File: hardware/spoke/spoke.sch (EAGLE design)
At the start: 22 parts, among them IC1 7805, J1 AVR_SPI_PRG_6PTH, J2 POWER_JACKPTH, U1 ATMEGA328P_PDIP, U2 AT25M01-SHM-B, U3 NRF24L01+

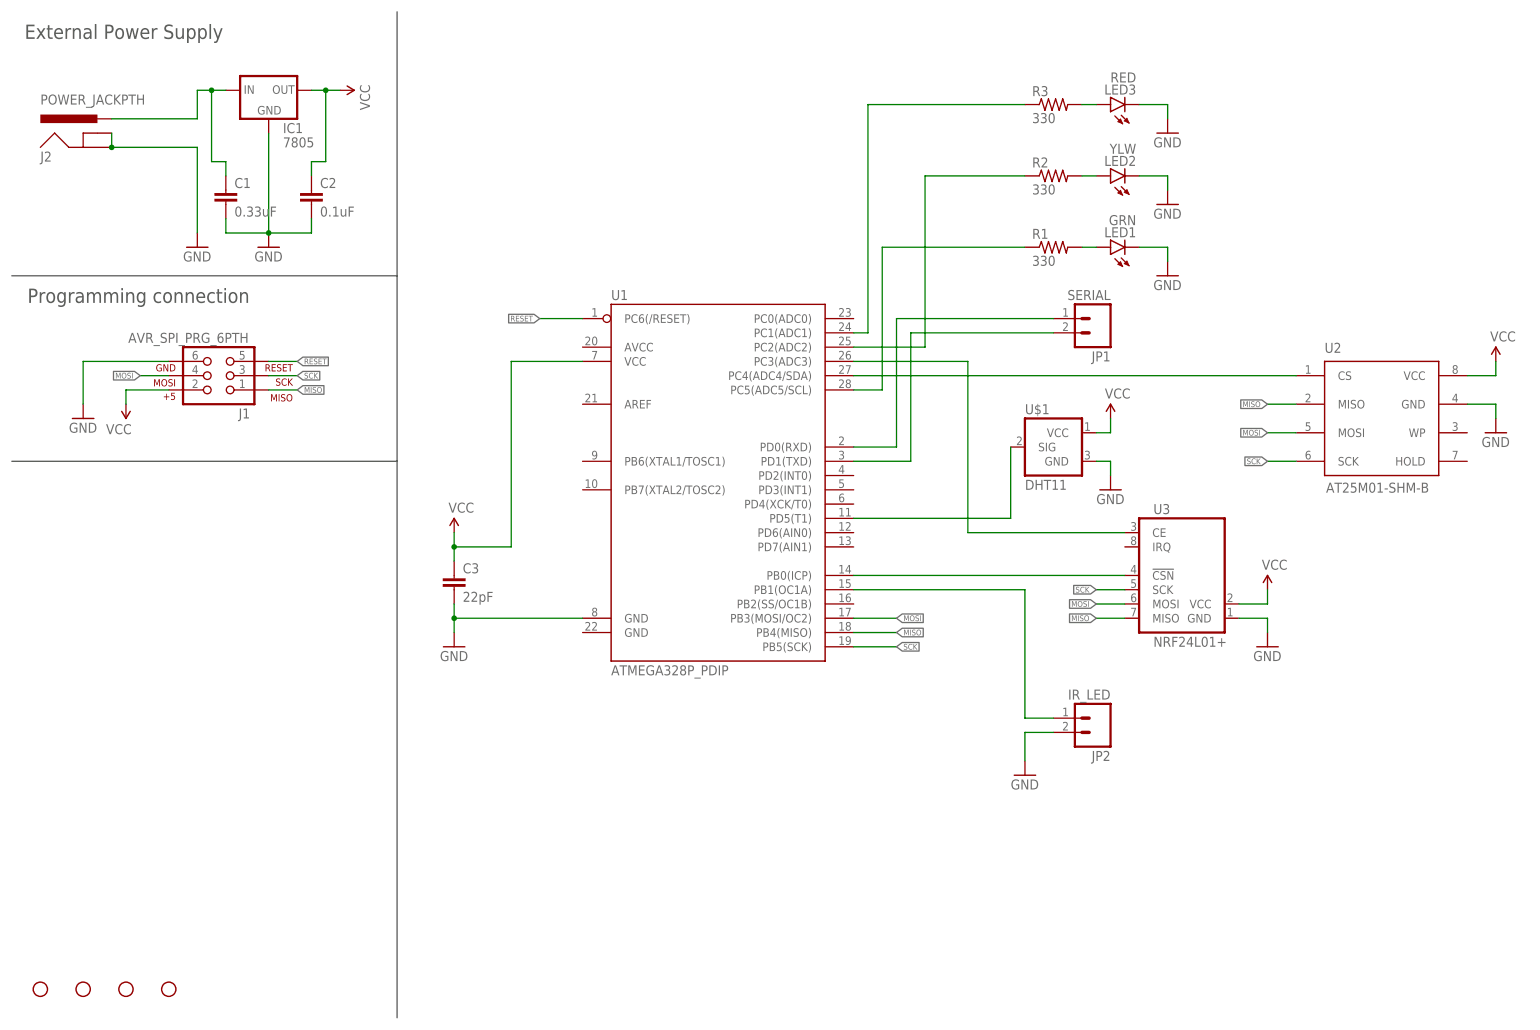
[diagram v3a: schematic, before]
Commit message: MOAR SMDs and 3.3v supply fixes
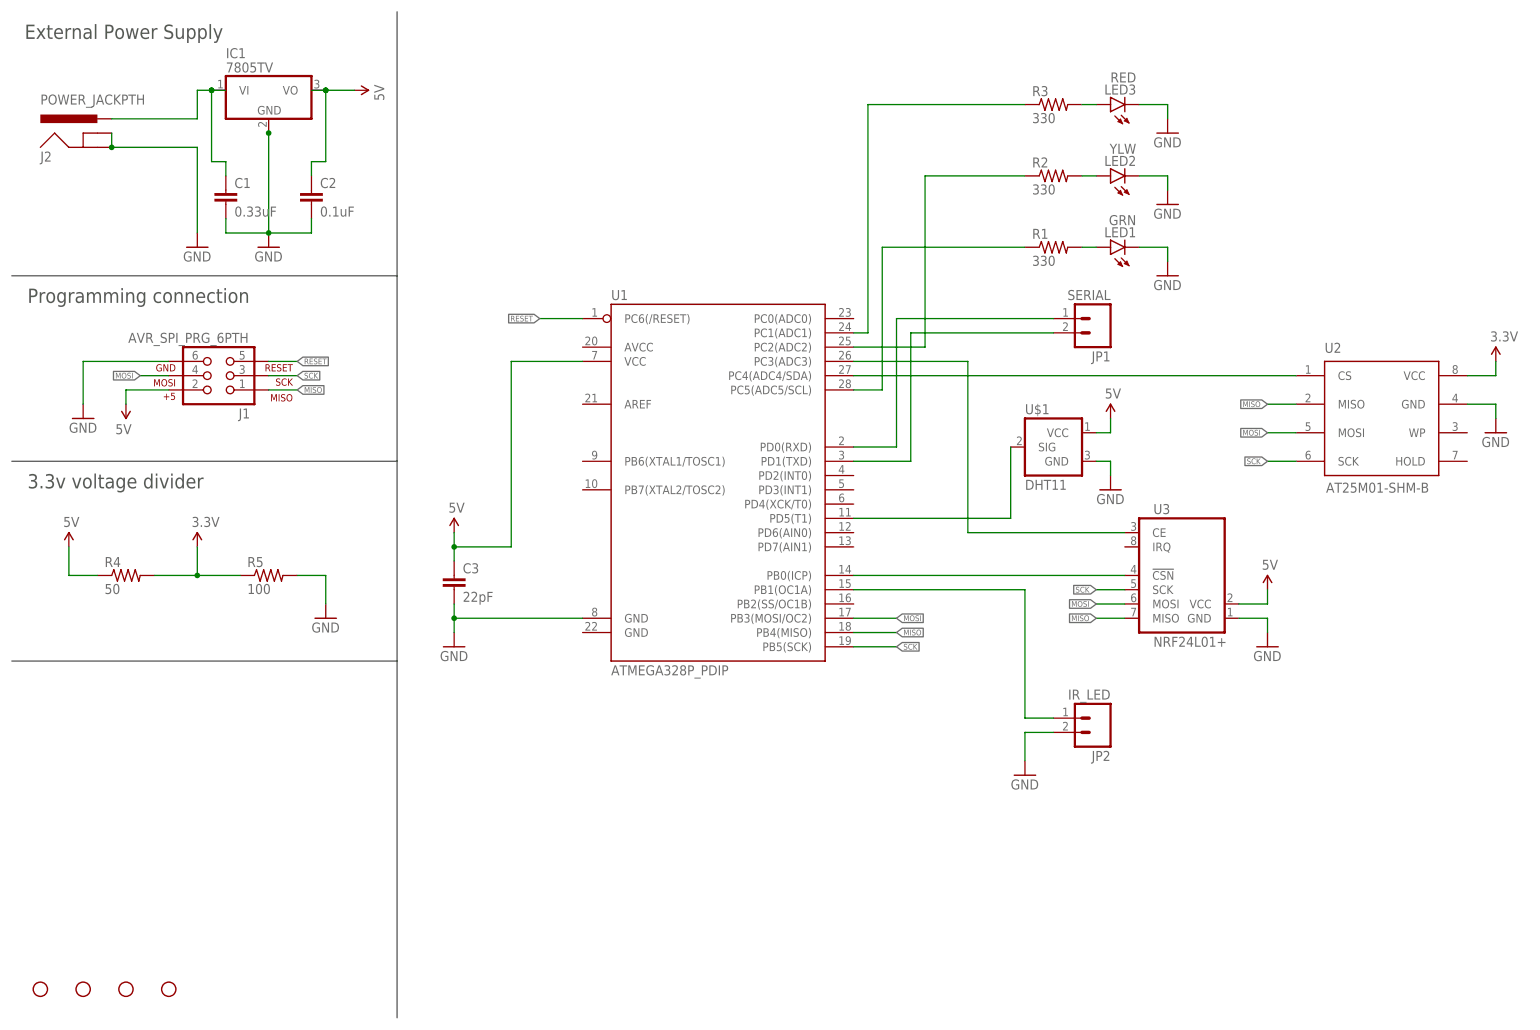
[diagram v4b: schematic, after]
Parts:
- added R4: 50, SparkFun-Passives:RESISTOR2010
- added R5: 100, SparkFun-Passives:RESISTOR2010
- C3: device SparkFun-Capacitors:CAPEZ -> SparkFun-Passives:CAP0805
- IC1: value 7805 -> 7805TV; device SparkFun-PowerIC:V_REG_78XXSINK -> linear:7805TV
- LED1, LED2, LED3: device SparkFun-LED:LED3MM -> SparkFun-LED:LED1206
- R1, R2, R3: device SparkFun-Passives:RESISTOREZ -> SparkFun-Passives:RESISTOR1206
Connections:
- removed net VCC: C2.1, C3.1, IC1.OUT, J1.2, U$1.VCC, U1.VCC, U2.VCC, U3.VCC
- new net 3.3V: R4.2, R5.1, U2.VCC
- new net 5V: C2.1, C3.1, IC1.VO, J1.2, R4.1, U$1.VCC, U1.VCC, U3.VCC
- net GND: now also R5.2
- net N$14: now also IC1.VI; no longer IC1.IN
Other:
- note added: "3.3v voltage divider"

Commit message: Update schematic from todos
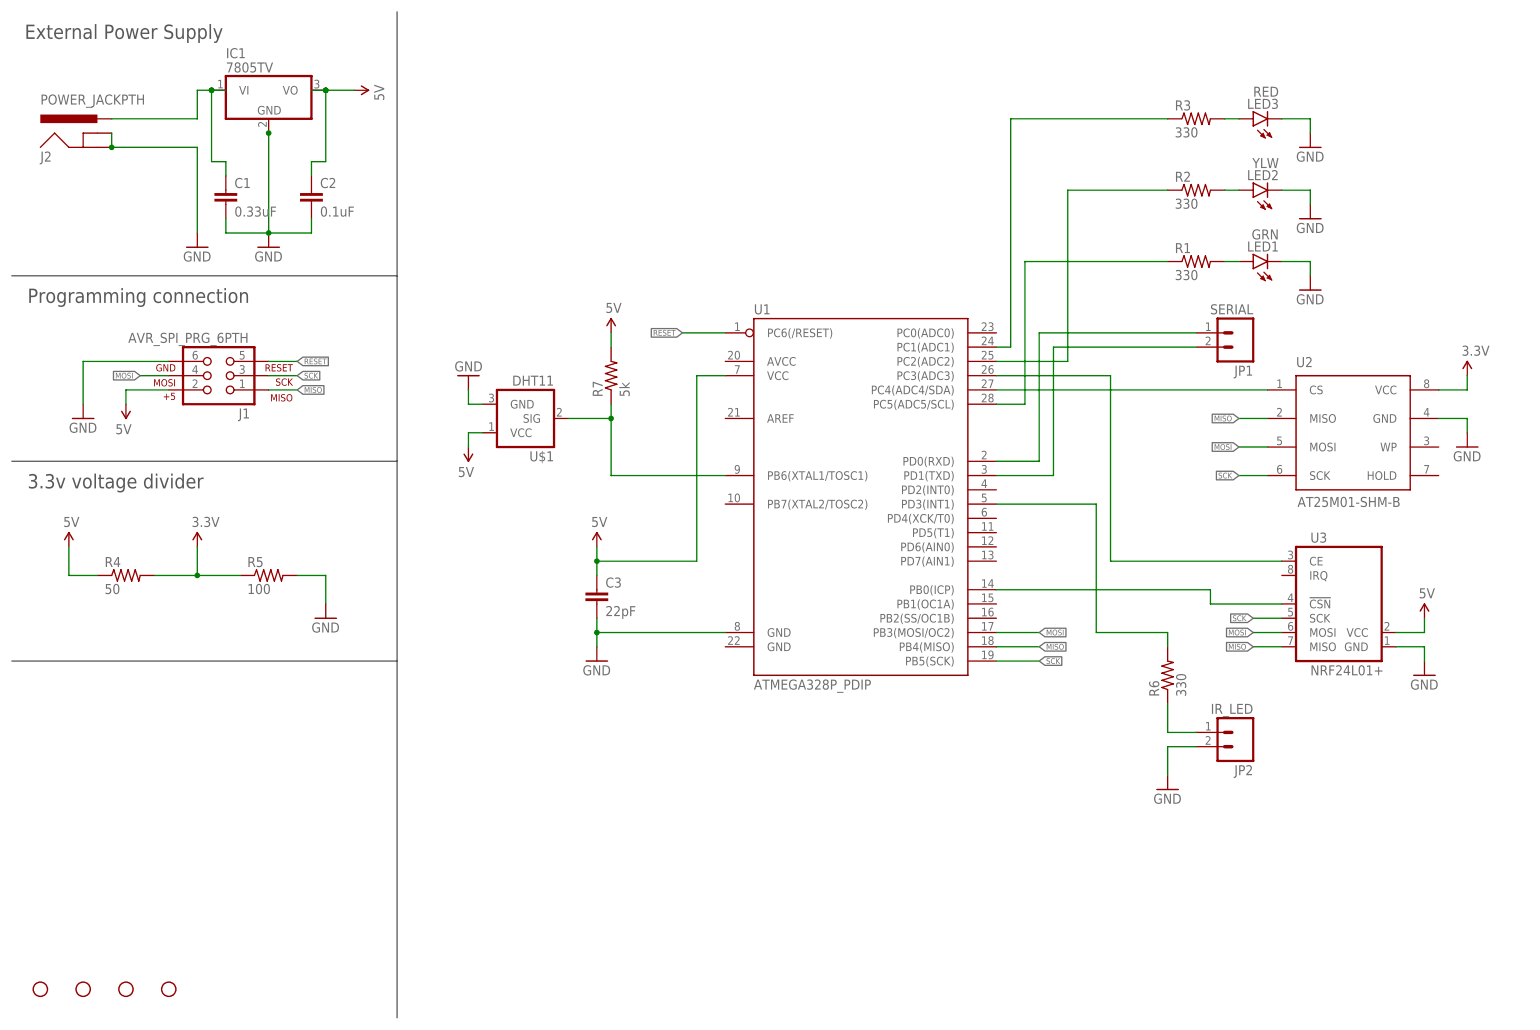
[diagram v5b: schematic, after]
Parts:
- added R6: 330, SparkFun-Passives:RESISTOR1206
- added R7: 5k, SparkFun-Passives:RESISTOR1206
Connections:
- removed net N$6: U$1.SIG, U1.PD5(T1)
- new net N$15: JP2.1, R6.1
- new net N$16: R6.2, U1.PD3(INT1)
- net 5V: now also R7.2
- net N$1: now also R7.1, U$1.SIG, U1.PB6(XTAL1/TOSC1); no longer JP2.1, U1.PB1(OC1A)
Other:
- moved on the sheet: C3, JP1, JP2, LED1, LED2, LED3, R1, R2, R3, U$1, U1, U2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

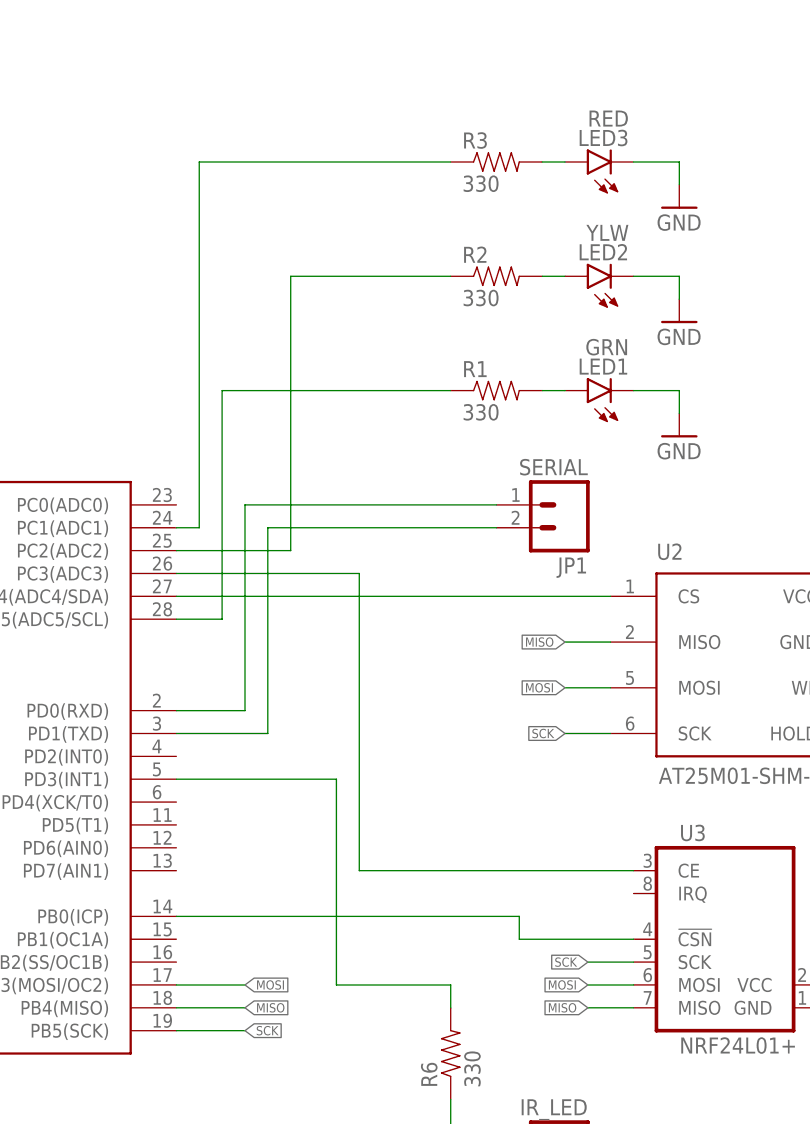
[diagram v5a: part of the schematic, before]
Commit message: Adjust schematic. Begin routing.
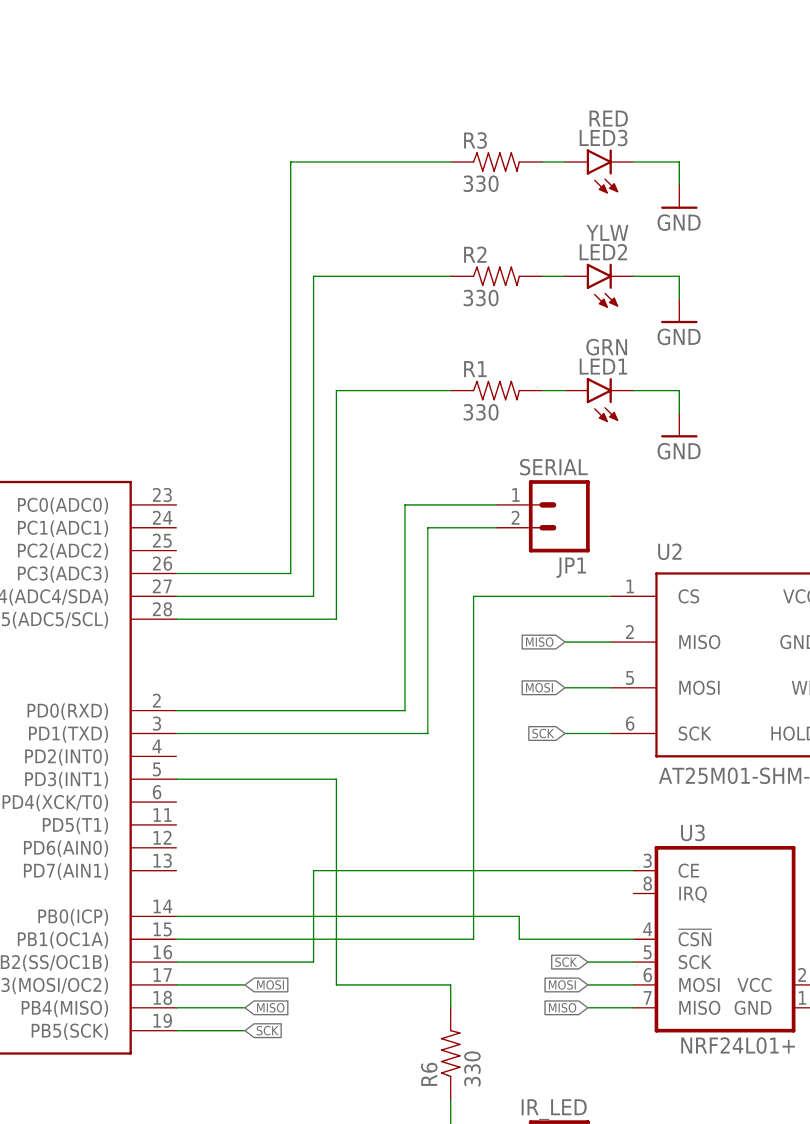
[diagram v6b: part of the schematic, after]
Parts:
- R1, R2, R3, R6, R7: device SparkFun-Passives:RESISTOR1206 -> SparkFun-Resistors:RESISTOR0805-RES
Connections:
- removed net N$13: R3.1, U1.PC1(ADC1)
- new net N$6: U1.PB1(OC1A), U2.CS
- net N$3: now also R2.1; no longer U2.CS
- net N$5: now also R3.1; no longer U3.CE
- net N$9: now also U1.PB2(SS/OC1B), U3.CE; no longer R2.1, U1.PC2(ADC2)
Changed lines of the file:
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@@
 <part name="GND8" library="SparkFun-Aesthetics" deviceset="GND" device=""/>
 <part name="LED1" library="SparkFun-LED" deviceset="LED" device="1206" value="GRN"/>
-<part name="R1" library="SparkFun-Passives" deviceset="RESISTOR" device="1206" value="330"/>
+<part name="R1" library="SparkFun-Resistors" deviceset="RESISTOR" device="0805-RES" value="330"/>
 <part name="GND9" library="SparkFun-Aesthetics" deviceset="GND" device=""/>
 <part name="LED2" library="SparkFun-LED" deviceset="LED" device="1206" value="YLW"/>
-<part name="R2" library="SparkFun-Passives" deviceset="RESISTOR" device="1206" value="330"/>
+<part name="R2" library="SparkFun-Resistors" deviceset="RESISTOR" device="0805-RES" value="330"/>
 <part name="GND10" library="SparkFun-Aesthetics" deviceset="GND" device=""/>
 <part name="LED3" library="SparkFun-LED" deviceset="LED" device="1206" value="RED"/>
-<part name="R3" library="SparkFun-Passives" deviceset="RESISTOR" device="1206" value="330"/>
+<part name="R3" library="SparkFun-Resistors" deviceset="RESISTOR" device="0805-RES" value="330"/>
 <part name="GND11" library="SparkFun-Aesthetics" deviceset="GND" device=""/>
 <part name="SUPPLY1" library="SparkFun-Aesthetics" deviceset="5V" device=""/>
@@
 <part name="SUPPLY7" library="SparkFun-Aesthetics" deviceset="5V" device=""/>
 <part name="SUPPLY8" library="SparkFun-Aesthetics" deviceset="3.3V" device=""/>
-<part name="R6" library="SparkFun-Passives" deviceset="RESISTOR" device="1206" value="330"/>
-<part name="R7" library="SparkFun-Passives" deviceset="RESISTOR" device="1206" value="5k"/>
+<part name="R6" library="SparkFun-Resistors" deviceset="RESISTOR" device="0805-RES" value="330"/>
+<part name="R7" library="SparkFun-Resistors" deviceset="RESISTOR" device="0805-RES" value="5k"/>
 <part name="SUPPLY9" library="SparkFun-Aesthetics" deviceset="5V" device=""/>
 <part name="U2" library="aurai" deviceset="AT25M01" device="-SHM-B"/>
@@
 <segment>
 <pinref part="JP1" gate="G$1" pin="1"/>
-<wire x1="210.82" y1="121.92" x2="182.88" y2="121.92" width="0.1524" layer="91"/>
-<wire x1="182.88" y1="121.92" x2="182.88" y2="99.06" width="0.1524" layer="91"/>
+<wire x1="210.82" y1="121.92" x2="200.66" y2="121.92" width="0.1524" layer="91"/>
+<wire x1="200.66" y1="121.92" x2="200.66" y2="99.06" width="0.1524" layer="91"/>
 <pinref part="U1" gate="G$1" pin="PD0(RXD)"/>
-<wire x1="182.88" y1="99.06" x2="175.26" y2="99.06" width="0.1524" layer="91"/>
+<wire x1="200.66" y1="99.06" x2="175.26" y2="99.06" width="0.1524" layer="91"/>
 </segment>
 </net>
@@
 <segment>
 <pinref part="U1" gate="G$1" pin="PD1(TXD)"/>
-<wire x1="175.26" y1="96.52" x2="185.42" y2="96.52" width="0.1524" layer="91"/>
-<wire x1="185.42" y1="96.52" x2="185.42" y2="119.38" width="0.1524" layer="91"/>
+<wire x1="175.26" y1="96.52" x2="203.2" y2="96.52" width="0.1524" layer="91"/>
+<wire x1="203.2" y1="96.52" x2="203.2" y2="119.38" width="0.1524" layer="91"/>
 <pinref part="JP1" gate="G$1" pin="2"/>
-<wire x1="185.42" y1="119.38" x2="210.82" y2="119.38" width="0.1524" layer="91"/>
+<wire x1="203.2" y1="119.38" x2="210.82" y2="119.38" width="0.1524" layer="91"/>
 </segment>
 </net>
@@
 <net name="N$12" class="0">
 <segment>
+<pinref part="U1" gate="G$1" pin="PC5(ADC5/SCL)"/>
+<wire x1="193.04" y1="109.22" x2="175.26" y2="109.22" width="0.1524" layer="91"/>
+<wire x1="193.04" y1="109.22" x2="193.04" y2="134.62" width="0.1524" layer="91"/>
 <pinref part="R1" gate="G$1" pin="1"/>
-<wire x1="205.74" y1="134.62" x2="180.34" y2="134.62" width="0.1524" layer="91"/>
-<wire x1="180.34" y1="134.62" x2="180.34" y2="109.22" width="0.1524" layer="91"/>
-<pinref part="U1" gate="G$1" pin="PC5(ADC5/SCL)"/>
-<wire x1="180.34" y1="109.22" x2="175.26" y2="109.22" width="0.1524" layer="91"/>
-</segment>
-</net>
-<net name="N$3" class="0">
-<segment>
-<pinref part="U1" gate="G$1" pin="PC4(ADC4/SDA)"/>
-<wire x1="223.52" y1="111.76" x2="175.26" y2="111.76" width="0.1524" layer="91"/>
-<pinref part="U2" gate="U1" pin="CS"/>
-</segment>
-</net>
-<net name="N$5" class="0">
-<segment>
-<pinref part="U1" gate="G$1" pin="PC3(ADC3)"/>
-<wire x1="175.26" y1="114.3" x2="195.58" y2="114.3" width="0.1524" layer="91"/>
-<wire x1="195.58" y1="114.3" x2="195.58" y2="81.28" width="0.1524" layer="91"/>
-<pinref part="U3" gate="U1" pin="CE"/>
-<wire x1="226.06" y1="81.28" x2="195.58" y2="81.28" width="0.1524" layer="91"/>
+<wire x1="193.04" y1="134.62" x2="205.74" y2="134.62" width="0.1524" layer="91"/>
 </segment>
 </net>
@@
 </segment>
 </net>
-<net name="N$9" class="0">
-<segment>
-<pinref part="R2" gate="G$1" pin="1"/>
-<wire x1="205.74" y1="147.32" x2="187.96" y2="147.32" width="0.1524" layer="91"/>
-<wire x1="187.96" y1="147.32" x2="187.96" y2="116.84" width="0.1524" layer="91"/>
-<pinref part="U1" gate="G$1" pin="PC2(ADC2)"/>
-<wire x1="187.96" y1="116.84" x2="175.26" y2="116.84" width="0.1524" layer="91"/>
-</segment>
-</net>
 <net name="N$11" class="0">
 <segment>
@@
 <pinref part="LED3" gate="G$1" pin="A"/>
 <wire x1="215.9" y1="160.02" x2="218.44" y2="160.02" width="0.1524" layer="91"/>
-</segment>
-</net>
-<net name="N$13" class="0">
-<segment>
-<pinref part="R3" gate="G$1" pin="1"/>
-<wire x1="205.74" y1="160.02" x2="177.8" y2="160.02" width="0.1524" layer="91"/>
-<wire x1="177.8" y1="160.02" x2="177.8" y2="119.38" width="0.1524" layer="91"/>
-<pinref part="U1" gate="G$1" pin="PC1(ADC1)"/>
-<wire x1="177.8" y1="119.38" x2="175.26" y2="119.38" width="0.1524" layer="91"/>
 </segment>
 </net>
@@
 </segment>
 </net>
+<net name="N$3" class="0">
+<segment>
+<pinref part="R2" gate="G$1" pin="1"/>
+<wire x1="205.74" y1="147.32" x2="190.5" y2="147.32" width="0.1524" layer="91"/>
+<wire x1="190.5" y1="147.32" x2="190.5" y2="111.76" width="0.1524" layer="91"/>
+<pinref part="U1" gate="G$1" pin="PC4(ADC4/SDA)"/>
+<wire x1="190.5" y1="111.76" x2="175.26" y2="111.76" width="0.1524" layer="91"/>
+</segment>
+</net>
+<net name="N$5" class="0">
+<segment>
+<pinref part="U1" gate="G$1" pin="PC3(ADC3)"/>
+<wire x1="175.26" y1="114.3" x2="187.96" y2="114.3" width="0.1524" layer="91"/>
+<wire x1="187.96" y1="114.3" x2="187.96" y2="160.02" width="0.1524" layer="91"/>
+<pinref part="R3" gate="G$1" pin="1"/>
+<wire x1="187.96" y1="160.02" x2="205.74" y2="160.02" width="0.1524" layer="91"/>
+</segment>
+</net>
+<net name="N$6" class="0">
+<segment>
+<pinref part="U1" gate="G$1" pin="PB1(OC1A)"/>
+<wire x1="175.26" y1="73.66" x2="208.28" y2="73.66" width="0.1524" layer="91"/>
+<wire x1="208.28" y1="73.66" x2="208.28" y2="111.76" width="0.1524" layer="91"/>
+<pinref part="U2" gate="U1" pin="CS"/>
+<wire x1="208.28" y1="111.76" x2="223.52" y2="111.76" width="0.1524" layer="91"/>
+</segment>
+</net>
+<net name="N$9" class="0">
+<segment>
+<pinref part="U3" gate="U1" pin="CE"/>
+<wire x1="226.06" y1="81.28" x2="190.5" y2="81.28" width="0.1524" layer="91"/>
+<wire x1="190.5" y1="81.28" x2="190.5" y2="71.12" width="0.1524" layer="91"/>
+<pinref part="U1" gate="G$1" pin="PB2(SS/OC1B)"/>
+<wire x1="190.5" y1="71.12" x2="175.26" y2="71.12" width="0.1524" layer="91"/>
+</segment>
+</net>
 </nets>
 </sheet>
 </sheets>
+<errors>
+</errors>
 </schematic>
 </drawing>
